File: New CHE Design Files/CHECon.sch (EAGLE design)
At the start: 33 parts, among them U2 MAX232SOIC16, U3 RS485SOIC

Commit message: P1
P1, seems to have errors
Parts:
- added U$30: RA_BUTTON, KW2:RA_BUTTON
- added U$31: (no value), GW-devices:RF-R0805
- POSCON, SCANNER: MFGP (none) -> 0955016889
- U$1: MFGP (none) -> CLV1A-FKB-CK1N1G1BB7R4S3
- U$10: MFGP (none) -> DF12(3.0)-40DP-0.5V(86)
- U$11, U$12, U$17, U$21, U$22, U$23: MFGP (none) -> 0805YD105KAT2A
- U$13, U$14, U$15, U$16: MFGP (none) -> TL3301DF260QG
- U$18, U$19, U$20: MFGP (none) -> CRCW080524R0JNEA
- U$2: MFGP (none) -> 52745-1097
- U$24: MFGP (none) -> 0805YD104KAT2A
- U$25, U$26, U$27, U$28, U$29, U$6: MFGP (none) -> CRCW080510K0FKEB
- U$3: MFGP (none) -> 3220-20-0100-00
- U$7: MFGP (none) -> C0805C106M4PACTU
- U$8: MFGP (none) -> WS2801
- U$9: MFGP (none) -> PJ-002A
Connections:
- net +3V3: now also U$31.2; no longer U$17.1, U$2.P$5, U$2.P$6, U$2.P$7, U$24.1, U$7.1
- net GND: now also U$3.P$15, U$3.P$17, U$3.P$19, U$3.P$3, U$3.P$5, U$3.P$9, U$30.1
- net N$24: no longer U3.VCC
- net N$34: no longer U$16.3
- net N$35: no longer U$15.3
- net N$36: no longer U$14.3
- net N$37: no longer U$13.3
- net N$7: now also U$10.PTE17/ADC0_SE5A/SPI0_SCK/UART2_RX/FTM_CLKIN1/LPTMR0_ALT3, U$30.2, U$31.1; no longer U$3.P$15, U$3.P$17, U$3.P$19, U$3.P$3, U$3.P$5, U$3.P$9
- net V+: now also U$17.1, U$2.P$5, U$2.P$6, U$2.P$7, U$24.1, U$7.1, U3.VCC

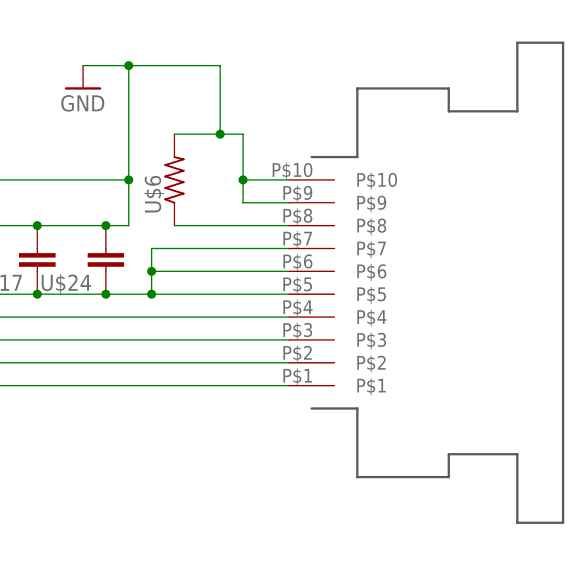
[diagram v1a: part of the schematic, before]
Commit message: Updated FPC
Pin names
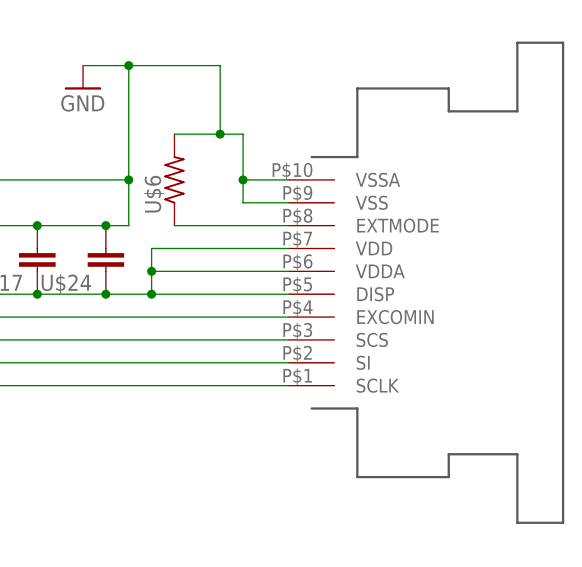
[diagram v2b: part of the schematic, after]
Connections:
- net GND: now also U$2.VSS, U$2.VSSA; no longer U$2.P$10, U$2.P$9
- net N$29: now also U$2.SI; no longer U$2.P$2
- net N$30: now also U$2.SCLK; no longer U$2.P$1
- net N$31: now also U$2.SCS; no longer U$2.P$3
- net N$32: now also U$2.EXTMODE; no longer U$2.P$8
- net N$33: now also U$2.EXCOMIN; no longer U$2.P$4
- net V+: now also U$2.DISP, U$2.VDD, U$2.VDDA; no longer U$2.P$5, U$2.P$6, U$2.P$7
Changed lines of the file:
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@@
 </segment>
 <segment>
-<pinref part="U$2" gate="G$1" pin="P$10"/>
+<pinref part="U$2" gate="G$1" pin="VSSA"/>
 <wire x1="-55.88" y1="154.94" x2="-60.96" y2="154.94" width="0.1524" layer="91"/>
 <wire x1="-60.96" y1="154.94" x2="-60.96" y2="152.4" width="0.1524" layer="91"/>
-<pinref part="U$2" gate="G$1" pin="P$9"/>
+<pinref part="U$2" gate="G$1" pin="VSS"/>
 <wire x1="-60.96" y1="152.4" x2="-55.88" y2="152.4" width="0.1524" layer="91"/>
 <wire x1="-60.96" y1="154.94" x2="-60.96" y2="160.02" width="0.1524" layer="91"/>
@@
 </segment>
 <segment>
-<pinref part="U$2" gate="G$1" pin="P$5"/>
+<pinref part="U$2" gate="G$1" pin="DISP"/>
 <wire x1="-55.88" y1="142.24" x2="-71.12" y2="142.24" width="0.1524" layer="91"/>
 <wire x1="-71.12" y1="142.24" x2="-76.2" y2="142.24" width="0.1524" layer="91"/>
@@
 <wire x1="-96.52" y1="142.24" x2="-96.52" y2="149.86" width="0.1524" layer="91"/>
 <pinref part="U$7" gate="G$1" pin="1"/>
-<pinref part="U$2" gate="G$1" pin="P$7"/>
+<pinref part="U$2" gate="G$1" pin="VDD"/>
 <wire x1="-55.88" y1="147.32" x2="-68.58" y2="147.32" width="0.1524" layer="91"/>
 <wire x1="-68.58" y1="147.32" x2="-71.12" y2="147.32" width="0.1524" layer="91"/>
 <wire x1="-71.12" y1="147.32" x2="-71.12" y2="144.78" width="0.1524" layer="91"/>
-<pinref part="U$2" gate="G$1" pin="P$6"/>
+<pinref part="U$2" gate="G$1" pin="VDDA"/>
 <wire x1="-71.12" y1="144.78" x2="-55.88" y2="144.78" width="0.1524" layer="91"/>
 <wire x1="-71.12" y1="144.78" x2="-71.12" y2="142.24" width="0.1524" layer="91"/>
@@
 <wire x1="-160.02" y1="124.46" x2="-96.52" y2="124.46" width="0.1524" layer="91"/>
 <wire x1="-96.52" y1="124.46" x2="-96.52" y2="134.62" width="0.1524" layer="91"/>
-<pinref part="U$2" gate="G$1" pin="P$2"/>
+<pinref part="U$2" gate="G$1" pin="SI"/>
 <wire x1="-96.52" y1="134.62" x2="-55.88" y2="134.62" width="0.1524" layer="91"/>
 </segment>
@@
 <wire x1="-160.02" y1="121.92" x2="-93.98" y2="121.92" width="0.1524" layer="91"/>
 <wire x1="-93.98" y1="121.92" x2="-93.98" y2="132.08" width="0.1524" layer="91"/>
-<pinref part="U$2" gate="G$1" pin="P$1"/>
+<pinref part="U$2" gate="G$1" pin="SCLK"/>
 <wire x1="-93.98" y1="132.08" x2="-55.88" y2="132.08" width="0.1524" layer="91"/>
 </segment>
@@
 <wire x1="-160.02" y1="119.38" x2="-101.6" y2="119.38" width="0.1524" layer="91"/>
 <wire x1="-101.6" y1="119.38" x2="-101.6" y2="137.16" width="0.1524" layer="91"/>
-<pinref part="U$2" gate="G$1" pin="P$3"/>
+<pinref part="U$2" gate="G$1" pin="SCS"/>
 <wire x1="-101.6" y1="137.16" x2="-55.88" y2="137.16" width="0.1524" layer="91"/>
 </segment>
@@
 <net name="N$32" class="2">
 <segment>
-<pinref part="U$2" gate="G$1" pin="P$8"/>
+<pinref part="U$2" gate="G$1" pin="EXTMODE"/>
 <pinref part="U$6" gate="G$1" pin="1"/>
 <wire x1="-55.88" y1="149.86" x2="-68.58" y2="149.86" width="0.1524" layer="91"/>
@@
 <net name="N$33" class="2">
 <segment>
-<pinref part="U$2" gate="G$1" pin="P$4"/>
+<pinref part="U$2" gate="G$1" pin="EXCOMIN"/>
 <pinref part="U$25" gate="G$1" pin="1"/>
 <wire x1="-55.88" y1="139.7" x2="-104.14" y2="139.7" width="0.1524" layer="91"/>

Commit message: P2
Fixed LED, reset switch, scanner RTS, flipped FPC
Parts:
- removed U$31: (no value), GW-devices:RF-R0805
- U$2: value 52745-1097 -> (none)
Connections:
- new net N$41: U$10.PTE3/MADC0_DM1/SPI1_SIN/!UART1_RTS!/MTRACE_D1/SPI1_SOUT, U2.T2IN
- net +3V3: no longer U$31.2
- net N$35: now also U$10.PTE17/ADC0_SE5A/SPI0_SCK/UART2_RX/FTM_CLKIN1/LPTMR0_ALT3; no longer U$10.PTE3/MADC0_DM1/SPI1_SIN/!UART1_RTS!/MTRACE_D1/SPI1_SOUT
- net N$6: now also U$30.2
- net N$7: now also SCANNER.6, U2.T2OUT; no longer U$10.PTE17/ADC0_SE5A/SPI0_SCK/UART2_RX/FTM_CLKIN1/LPTMR0_ALT3, U$30.2, U$31.1
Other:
- note added: "P2: Fixed LED, reset switch, scanner RTS, flipped FPC pinout"
- moved on the sheet: U$30

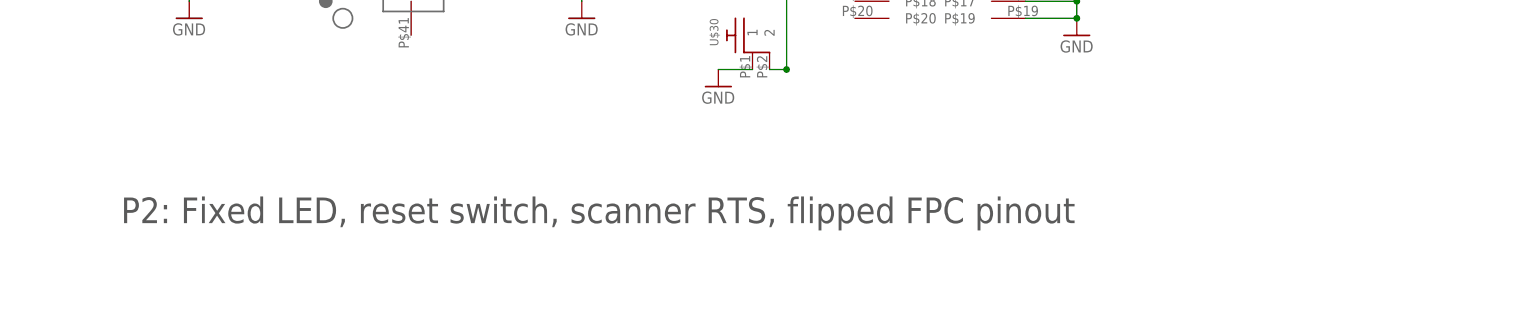
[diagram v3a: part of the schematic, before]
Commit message: P3 - in progress
Added 0.4mm spacing, need level shifter and other screen changes
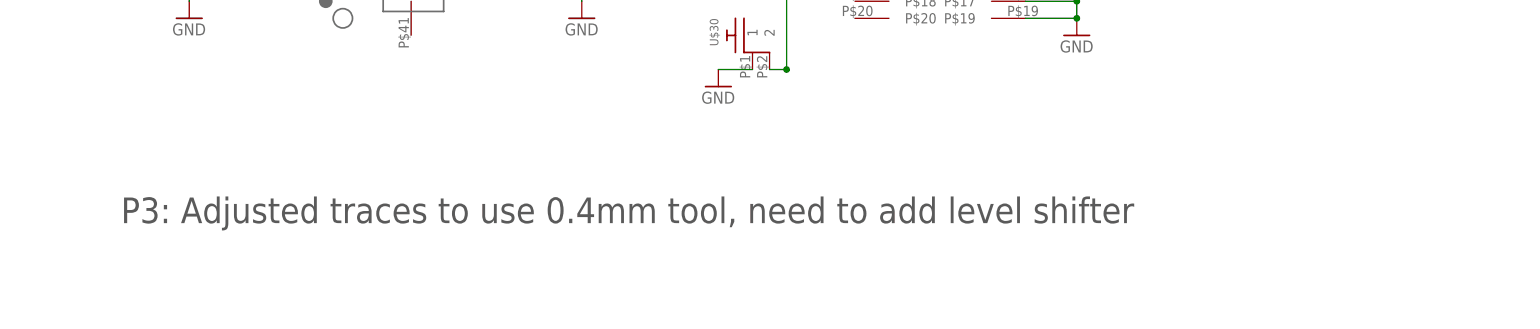
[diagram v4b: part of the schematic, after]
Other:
- note added: "P3: Adjusted traces to use 0.4mm tool, need to add level shifter"
- note removed: "P2: Fixed LED, reset switch, scanner RTS, flipped FPC pinout"
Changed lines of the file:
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@@
 <sheet>
 <plain>
-<text x="-218.44" y="55.88" size="3.81" layer="97">P2: Fixed LED, reset switch, scanner RTS, flipped FPC pinout</text>
+<text x="-218.44" y="55.88" size="3.81" layer="97">P3: Adjusted traces to use 0.4mm tool, need to add level shifter</text>
 </plain>
 <instances>
